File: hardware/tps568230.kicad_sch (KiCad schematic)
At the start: 20 parts, among them U1 TPS568230

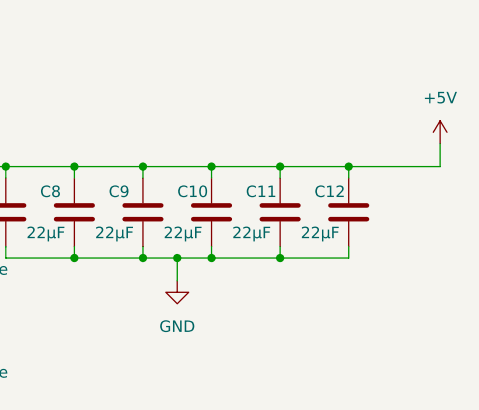
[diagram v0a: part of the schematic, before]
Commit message: First draft of audio amplifier
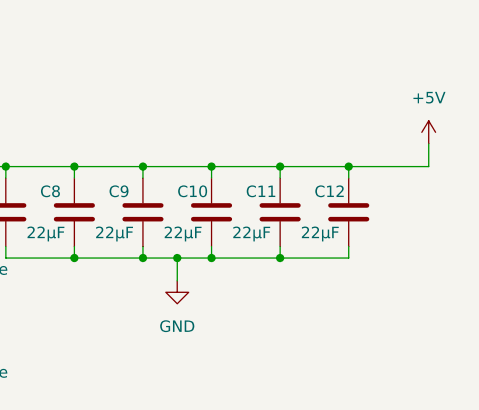
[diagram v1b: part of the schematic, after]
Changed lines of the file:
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@@
 	(wire
 		(pts
-			(xy 226.06 78.74) (xy 215.9 78.74)
+			(xy 224.79 78.74) (xy 215.9 78.74)
 		)
 		(stroke
@@
 	(wire
 		(pts
-			(xy 226.06 76.2) (xy 226.06 78.74)
+			(xy 224.79 76.2) (xy 224.79 78.74)
 		)
 		(stroke
@@
 	(symbol
 		(lib_id "power:+5V")
-		(at 226.06 76.2 0)
+		(at 224.79 76.2 0)
 		(unit 1)
 		(exclude_from_sim no)
@@
 		(fields_autoplaced yes)
 		(property "Reference" "#PWR010"
-			(at 226.06 80.01 0)
+			(at 224.79 80.01 0)
 			(effects
 				(font
@@
 		)
 		(property "Value" "+5V"
-			(at 226.06 71.12 0)
-			(effects
-				(font
-					(size 1.27 1.27)
-				)
-			)
-		)
-		(property "Footprint" ""
-			(at 226.06 76.2 0)
+			(at 224.79 71.12 0)
+			(effects
+				(font
+					(size 1.27 1.27)
+				)
+			)
+		)
+		(property "Footprint" ""
+			(at 224.79 76.2 0)
 			(effects
 				(font
@@
 		)
 		(property "Datasheet" ""
-			(at 226.06 76.2 0)
+			(at 224.79 76.2 0)
 			(effects
 				(font
@@
 		)
 		(property "Description" "Power symbol creates a global label with name \"+5V\""
-			(at 226.06 76.2 0)
-			(effects
-				(font
+			(at 224.79 76.2 0)
+			(effects
+				(font

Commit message: Updating peripherals
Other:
- company: (none) -> Chroma
- title: (none) -> Chromapi's Voltage Regulation
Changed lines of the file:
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@@
 	(generator_version "9.0")
 	(paper "A4")
+	(title_block
+		(title "Chromapi's Voltage Regulation")
+		(rev "v1.0.0")
+		(company "Chroma")
+		(comment 1 "Ousmane THIONGANE")
+	)
 	(junction
 		(at 163.83 78.74)

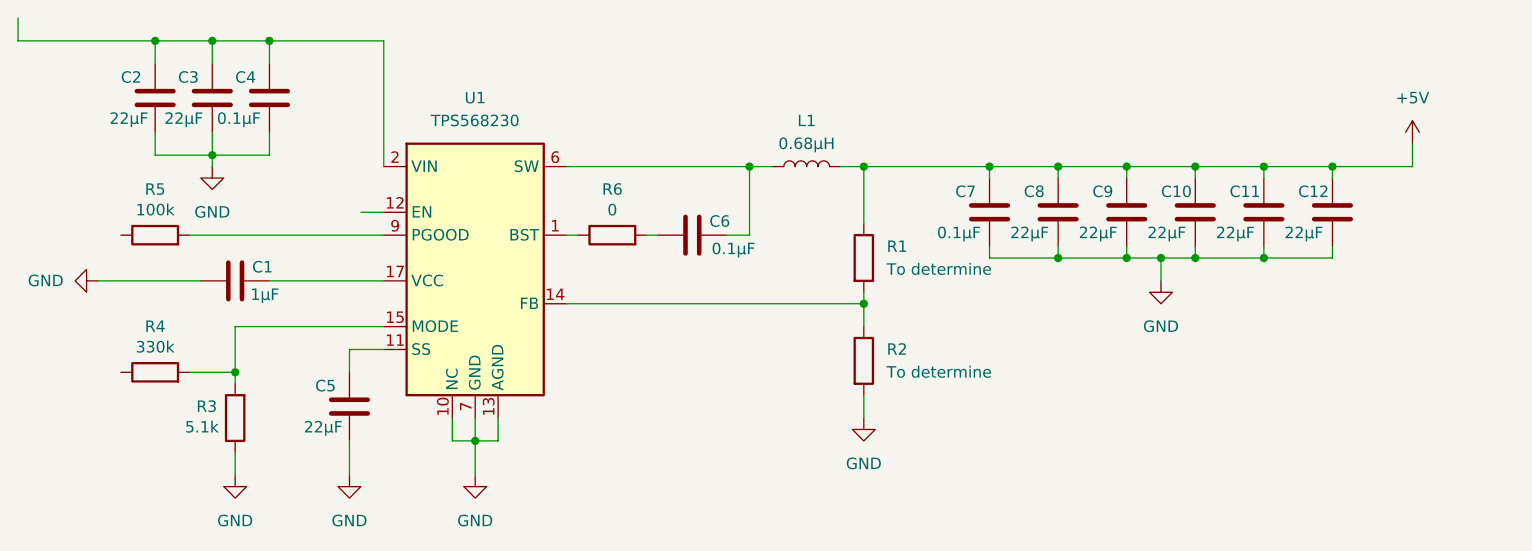
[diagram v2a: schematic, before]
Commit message: Component sizing in voltage regulator
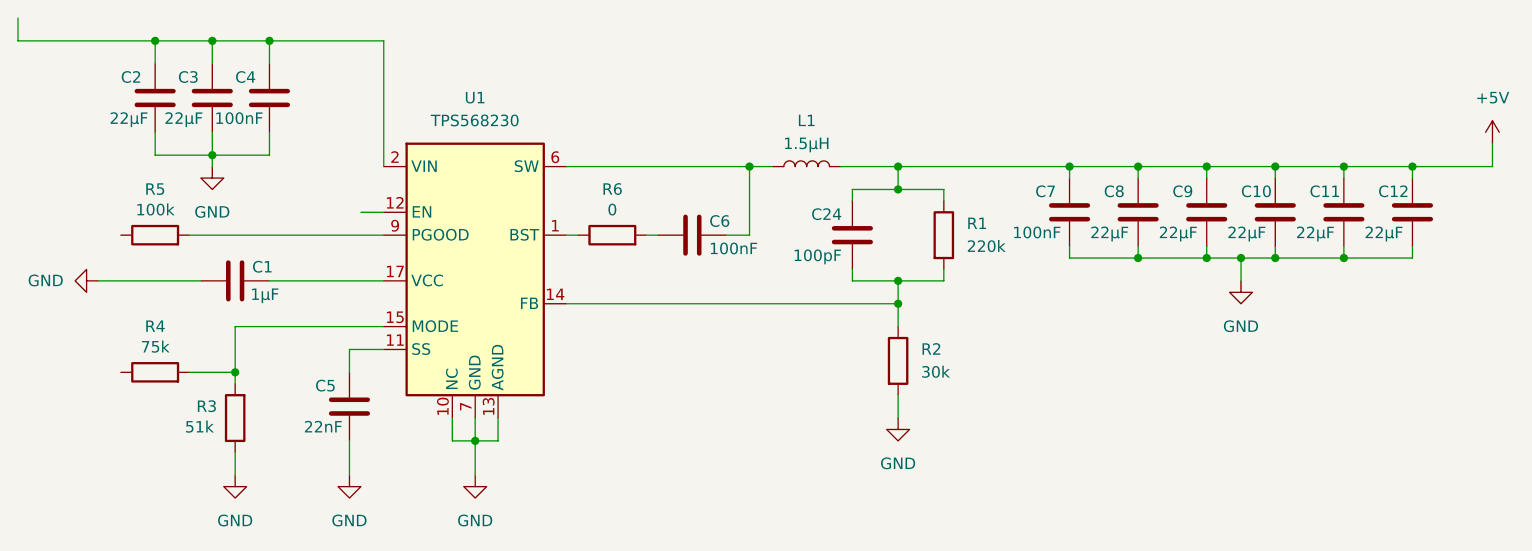
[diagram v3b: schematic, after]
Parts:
- added C24: 100pF, symbol Device:C
- C4, C6, C7: value 0.1µF -> 100nF
- C5: value 22µF -> 22nF
- L1: value 0.68µH -> 1.5µH
- R1: value To determine -> 220k
- R2: value To determine -> 30k
- R3: value 5.1k -> 51k
- R4: value 330k -> 75k
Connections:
- net +5V: now also C24.1
- net at R1.2, R2.1, U1.14 (FB): now also C24.2
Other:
- moved on the sheet: C10, C11, C12, C7, C8, C9, R1, R2

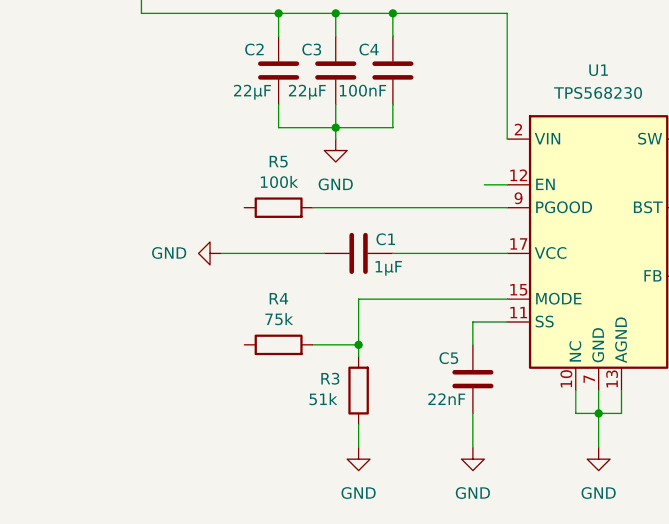
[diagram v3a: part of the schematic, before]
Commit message: Updating voltage regulation schematic
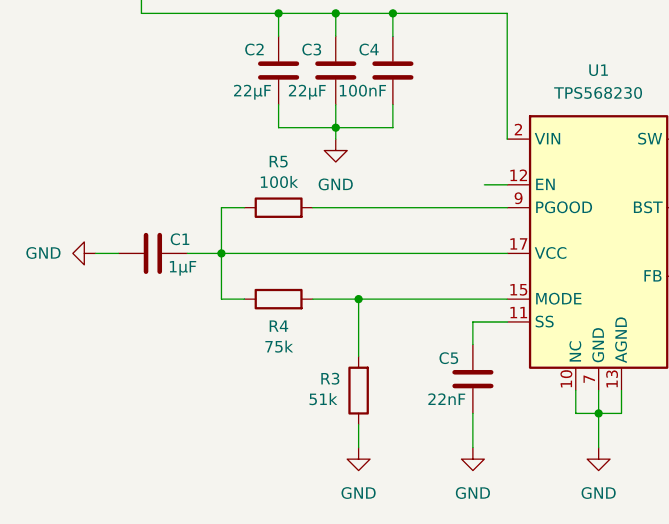
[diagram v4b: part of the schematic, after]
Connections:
- net at C1.1, U1.17 (VCC): now also R4.1, R5.1
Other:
- moved on the sheet: C1, R4
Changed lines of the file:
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@@
+	)
+	(junction
+		(at 93.98 96.52)
+		(diameter 0)
+		(color 0 0 0 0)
 	)
 	(junction
@@
 	)
 	(junction
-		(at 93.98 101.6)
-		(diameter 0)
-		(color 0 0 0 0)
-	)
-	(junction
 		(at 167.64 91.44)
 		(diameter 0)
@@
 	)
 	(junction
+		(at 78.74 91.44)
+		(diameter 0)
+		(color 0 0 0 0)
+	)
+	(junction
 		(at 201.93 88.9)
 		(diameter 0)
@@
 	(wire
 		(pts
-			(xy 78.74 91.44) (xy 90.17 91.44)
+			(xy 64.77 91.44) (xy 67.31 91.44)
 		)
 		(stroke
@@
 	(wire
 		(pts
-			(xy 93.98 101.6) (xy 93.98 102.87)
+			(xy 78.74 91.44) (xy 110.49 91.44)
+		)
+		(stroke
+			(width 0)
+			(type default)
+		)
+	)
+	(wire
+		(pts
+			(xy 93.98 96.52) (xy 93.98 102.87)
 		)
 		(stroke
@@
 	(wire
 		(pts
+			(xy 81.28 96.52) (xy 78.74 96.52)
+		)
+		(stroke
+			(width 0)
+			(type default)
+		)
+	)
+	(wire
+		(pts
 			(xy 172.72 81.28) (xy 172.72 82.55)
 		)
@@
 	(wire
 		(pts
+			(xy 78.74 96.52) (xy 78.74 91.44)
+		)
+		(stroke
+			(width 0)
+			(type default)
+		)
+	)
+	(wire
+		(pts
 			(xy 91.44 74.93) (xy 91.44 77.47)
 		)
@@
 	(wire
 		(pts
+			(xy 78.74 86.36) (xy 78.74 91.44)
+		)
+		(stroke
+			(width 0)
+			(type default)
+		)
+	)
+	(wire
+		(pts
 			(xy 120.65 106.68) (xy 120.65 109.22)
 		)
@@
 	(wire
 		(pts
+			(xy 81.28 86.36) (xy 78.74 86.36)
+		)
+		(stroke
+			(width 0)
+			(type default)
+		)
+	)
+	(wire
+		(pts
 			(xy 186.69 88.9) (xy 194.31 88.9)
 		)
@@
 	(wire
 		(pts
-			(xy 88.9 101.6) (xy 93.98 101.6)
+			(xy 88.9 96.52) (xy 93.98 96.52)
 		)
 		(stroke
@@
 	(wire
 		(pts
-			(xy 97.79 91.44) (xy 110.49 91.44)
+			(xy 74.93 91.44) (xy 78.74 91.44)
 		)
 		(stroke
@@
 		(pts
 			(xy 167.64 91.44) (xy 162.56 91.44)
-		)
-		(stroke
-			(width 0)
-			(type default)
-		)
-	)
-	(wire
-		(pts
-			(xy 93.98 96.52) (xy 93.98 101.6)
 		)
 		(stroke
@@
 	(symbol
 		(lib_id "Device:C")
-		(at 93.98 91.44 270)
+		(at 71.12 91.44 270)
 		(unit 1)
 		(exclude_from_sim no)
@@
 		(dnp no)
 		(property "Reference" "C1"
-			(at 97.028 89.916 90)
+			(at 74.168 89.916 90)
 			(effects
 				(font
@@
 		)
 		(property "Value" "1µF"
-			(at 97.282 92.964 90)
+			(at 74.422 92.964 90)
 			(effects
 				(font
@@
 		)
 		(property "Footprint" ""
-			(at 90.17 92.4052 0)
+			(at 67.31 92.4052 0)
 			(effects
 				(font
@@
 		)
 		(property "Datasheet" "~"
-			(at 93.98 91.44 0)
+			(at 71.12 91.44 0)
 			(effects
 				(font
@@
 		)
 		(property "Description" "Unpolarized capacitor"
-			(at 93.98 91.44 0)
+			(at 71.12 91.44 0)
 			(effects
 				(font
@@
 	(symbol
 		(lib_id "Device:R")
-		(at 85.09 101.6 90)
+		(at 85.09 96.52 90)
 		(unit 1)
 		(exclude_from_sim no)
@@
 		(dnp no)
 		(property "Reference" "R4"
-			(at 85.09 96.52 90)
+			(at 85.09 99.568 90)
 			(effects
 				(font
@@
 		)
 		(property "Value" "75k"
-			(at 85.09 98.806 90)
+			(at 85.09 101.854 90)
 			(effects
 				(font
@@
 		)
 		(property "Footprint" ""
-			(at 85.09 103.378 90)
+			(at 85.09 98.298 90)
 			(effects
 				(font
@@
 		)
 		(property "Datasheet" "~"
-			(at 85.09 101.6 0)
+			(at 85.09 96.52 0)
 			(effects
 				(font
@@
 		)
 		(property "Description" "Resistor"
-			(at 85.09 101.6 0)
+			(at 85.09 96.52 0)
 			(effects
 				(font
@@
 	(symbol
 		(lib_id "power:GND")
-		(at 78.74 91.44 270)
+		(at 64.77 91.44 270)
 		(unit 1)
 		(exclude_from_sim no)
@@
 		(fields_autoplaced yes)
 		(property "Reference" "#PWR02"
-			(at 72.39 91.44 0)
+			(at 58.42 91.44 0)
 			(effects
 				(font
@@
 		)
 		(property "Value" "GND"
-			(at 74.93 91.4399 90)
+			(at 60.96 91.4399 90)
 			(effects
 				(font
@@
 		)
 		(property "Footprint" ""
-			(at 78.74 91.44 0)
+			(at 64.77 91.44 0)
 			(effects
 				(font
@@
 		)
 		(property "Datasheet" ""
-			(at 78.74 91.44 0)
+			(at 64.77 91.44 0)
 			(effects
 				(font
@@
 		)
 		(property "Description" "Power symbol creates a global label with name \"GND\" , ground"
-			(at 78.74 91.44 0)
-			(effects
-				(font
+			(at 64.77 91.44 0)
+			(effects
+				(font

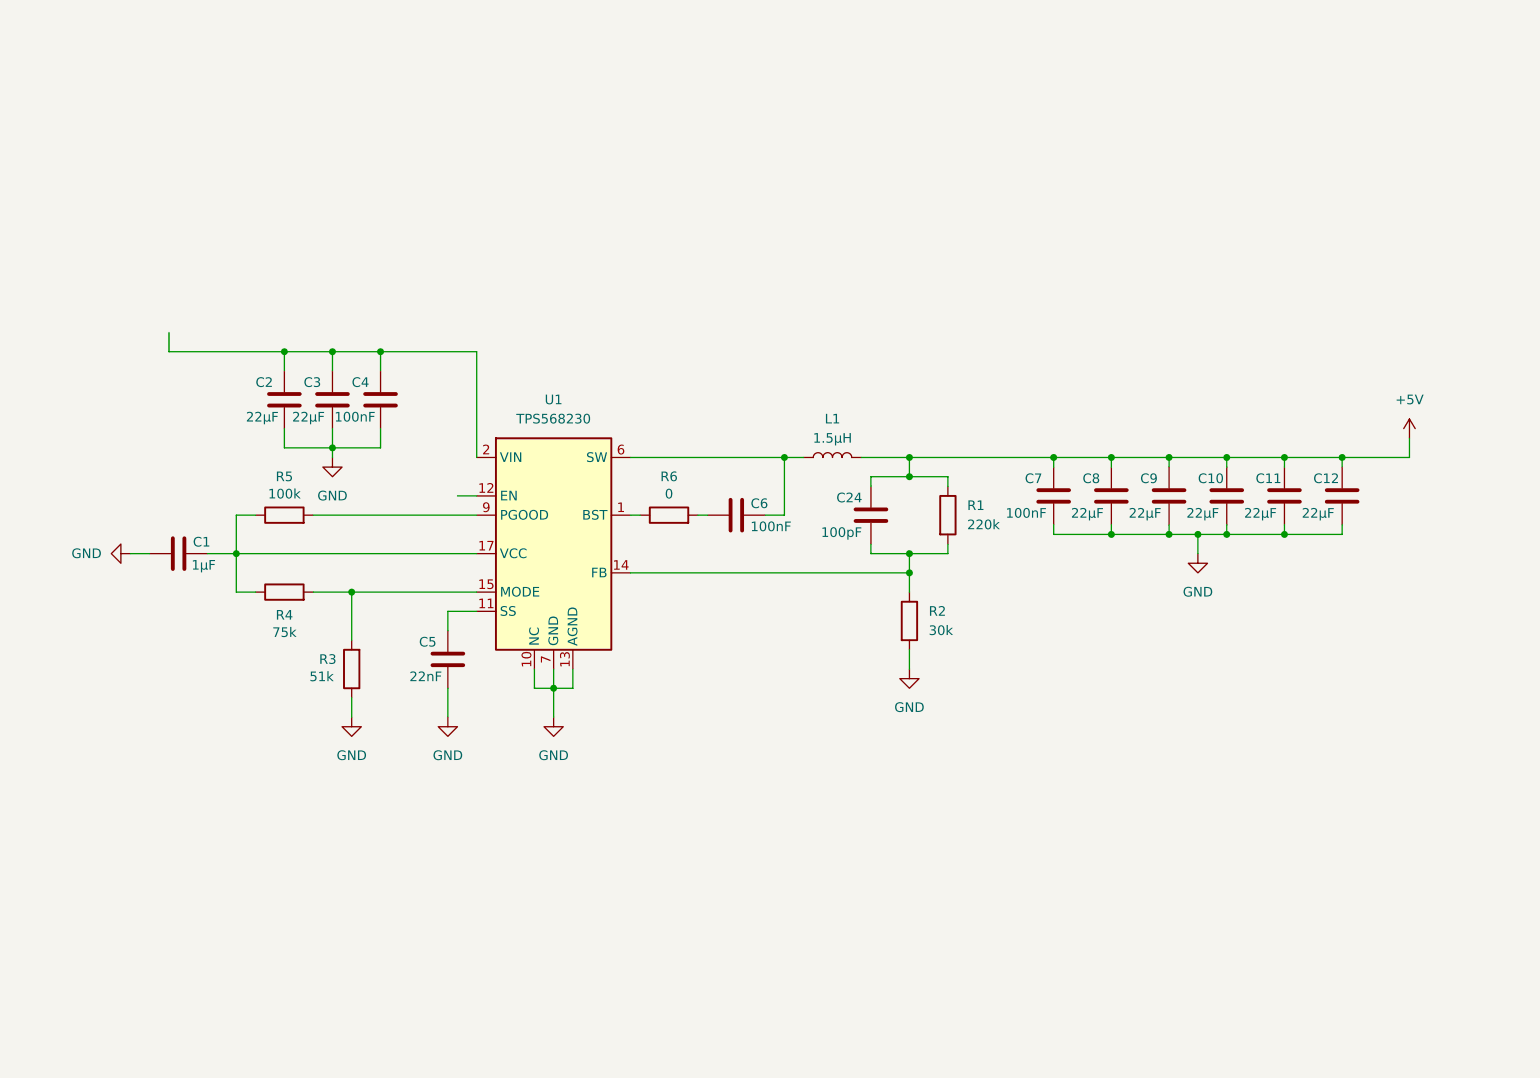
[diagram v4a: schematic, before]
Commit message: Adding 5V to 3V3 regulator
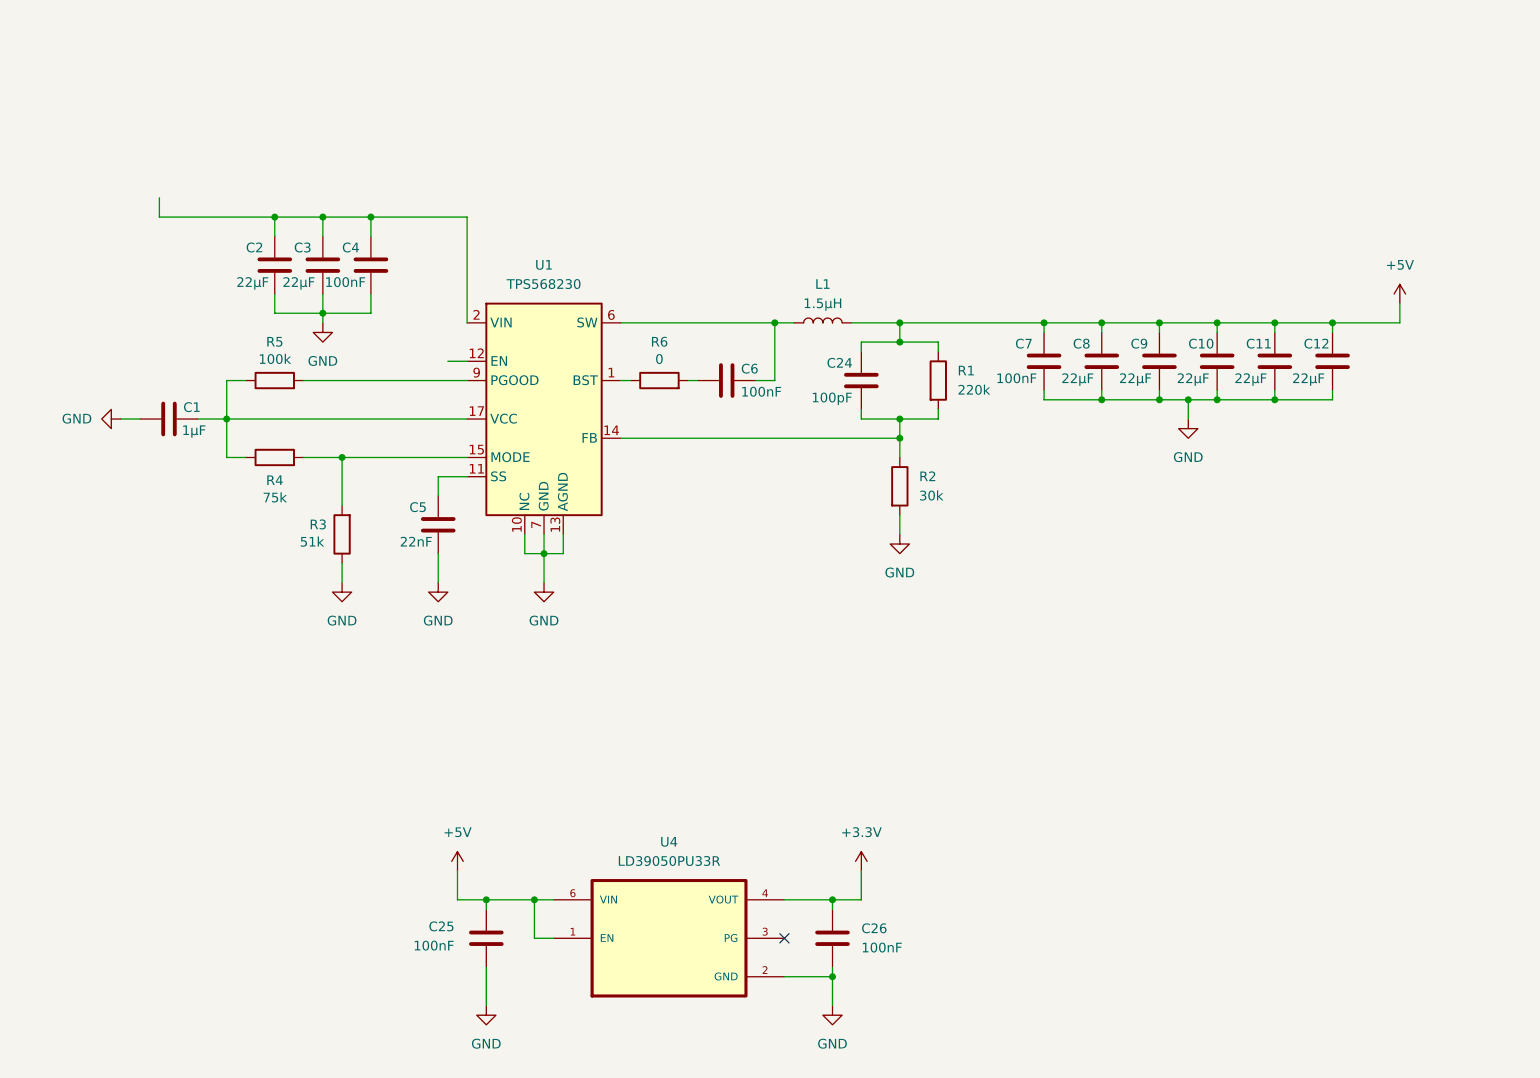
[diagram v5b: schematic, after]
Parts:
- added C25, C26: 100nF, symbol Device:C
- added U4: LD39050PU33R, LD39050PU33R:SON95P300X300X100-7N, symbol LD39050PU33R:LD39050PU33R
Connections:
- net +5V: now also C25.1, U4.1 (EN), U4.6 (VIN)
- net GND: now also C25.2, C26.2, U4.2 (GND), U4.7 (GND)
- new net +3.3V: C26.1, U4.4 (VOUT)
- no-connect marks 0 -> 1
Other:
- moved on the sheet: C1, C10, C11, C12, C2, C24, C3, C4, C5, C6, C7, C8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

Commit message: Adding BMS
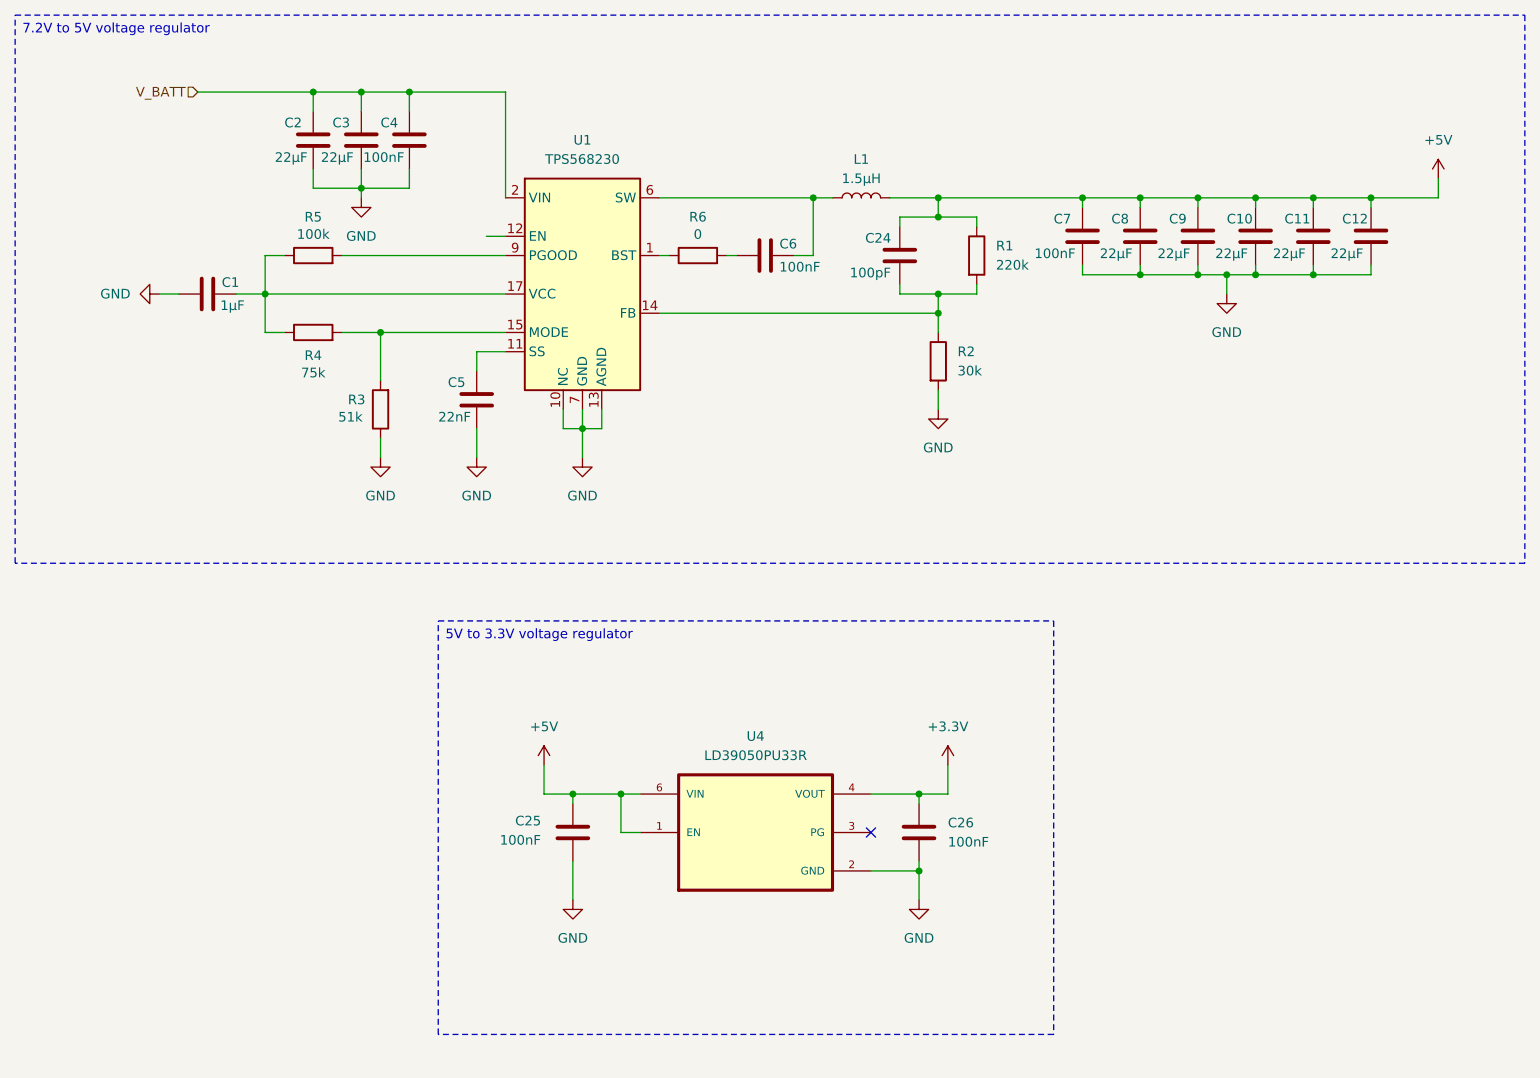
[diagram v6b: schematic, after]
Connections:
- net V_BATT: now reaches C2.1, C3.1, C4.1, U1.2 (VIN), U1.3 (VIN), U1.4 (VIN), U1.5 (VIN)
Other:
- moved on the sheet: C1, C10, C11, C12, C2, C24, C25, C26, C3, C4, C5, C6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
